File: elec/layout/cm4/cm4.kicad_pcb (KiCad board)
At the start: 2 copper layers, 4 parts, among them CN1 HRSHirose_DF40C_100DS_0_4V51, CN2 HRSHirose_DF40C_100DS_0_4V51, U1 _Texas_Instruments_SN74LVC1G0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

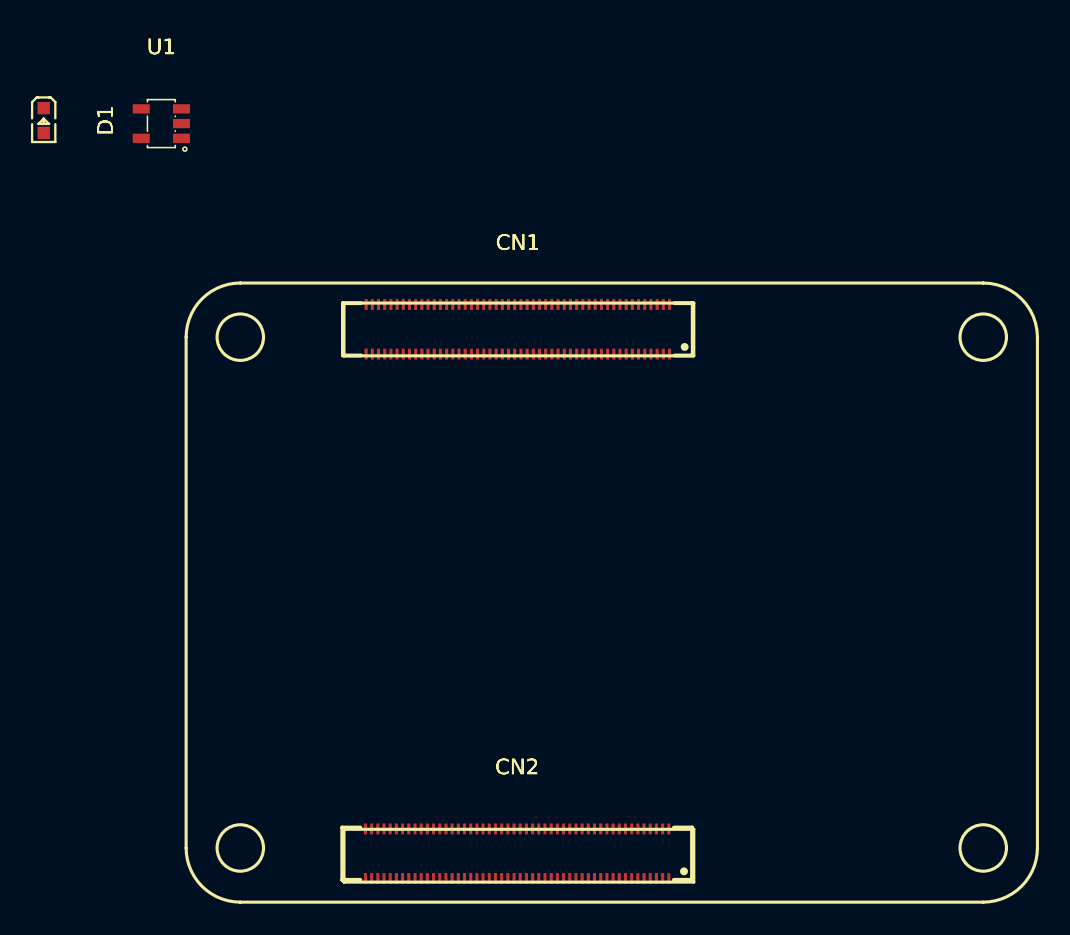
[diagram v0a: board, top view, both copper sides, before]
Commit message: add ethernet connector
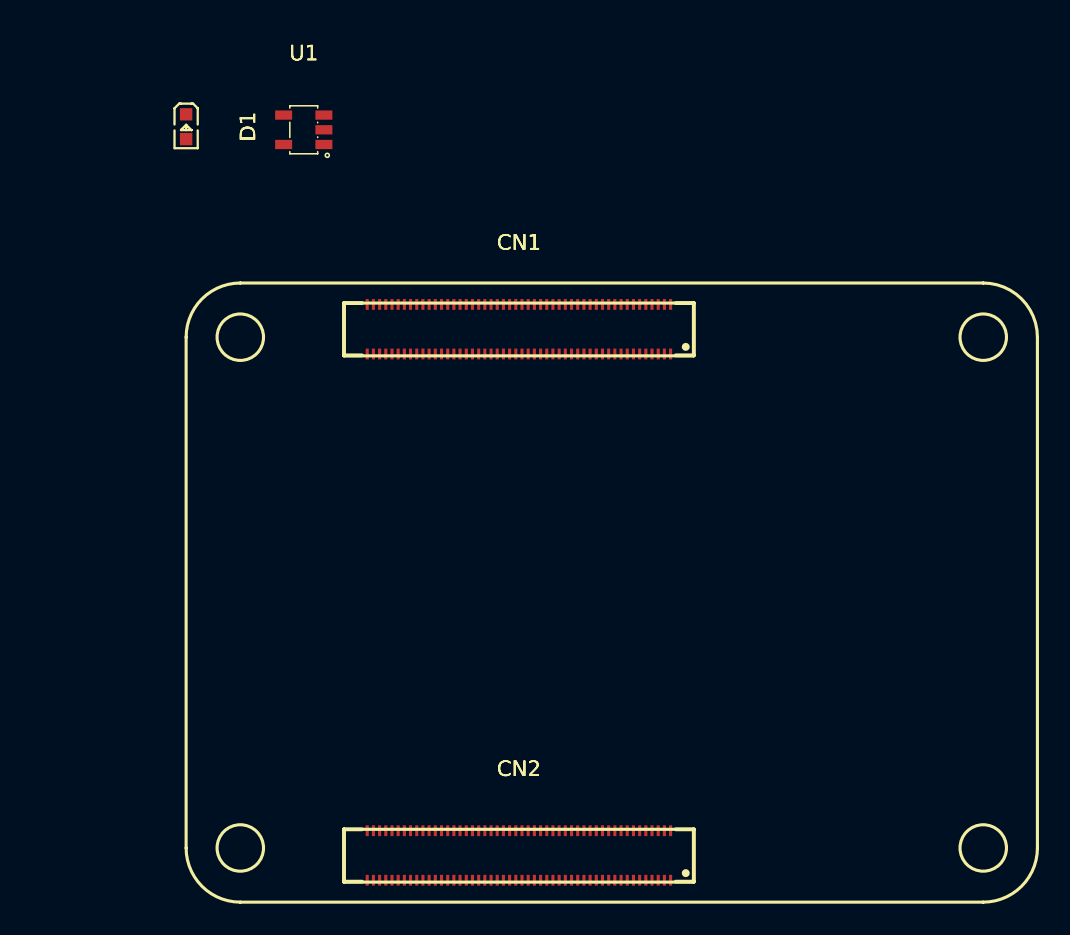
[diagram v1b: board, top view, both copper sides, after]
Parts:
- moved D1 9.21 mm to (128.4, 90.2)
- moved U1 9.21 mm to (136.0, 90.4)
- moved CN2 0.16 mm to (149.9, 137.3)
- moved CN1 0.07 mm to (149.9, 103.3)
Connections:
- net hdi_b-pins[28] renamed HDMI1_D0_P
- net hdi_b-pins[29] renamed HDMI1_D0_N
- net pins[2] renamed ETH_P1_N
- net pins[4] renamed ETH_P0_N
- net signal-11 renamed HDMI1_CEC
- CN1 pad 1: net -> GND
- CN1 pad 10: pins[9] -> pins[19]
- CN1 pad 100: hdi_a-pins[99] -> GND
- CN1 pad 11: pins[10] -> GND
- CN1 pad 12: pins[11] -> signal-2
- CN1 pad 13: net -> I2S_WS
- CN1 pad 14: net -> signal-4
- CN1 pad 15: pins[14] -> signal-3
- CN1 pad 16: hdi_a-pins[15] -> GND
- CN1 pad 17: pins[16] -> signal-1
- CN1 pad 18: hdi_a-pins[17] -> hdi_a-pins[35]
- CN1 pad 19: pins[18] -> pins[37]
- CN1 pad 2: net -> ETH_P1_P
- CN1 pad 20: pins[19] -> pins[39]
- CN1 pad 21: net -> GND
- CN1 pad 22: net -> pins[43]
- CN1 pad 23: net -> pins[45]
- CN1 pad 24: signal-7 -> signal
- CN1 pad 25: signal-4 -> pins[49]
- CN1 pad 26: signal-1 -> GND
- CN1 pad 27: pins[26] -> pins[53]
- CN1 pad 28: pins[27] -> signal-8
- CN1 pad 29: pins[28] -> pins[57]
- CN1 pad 30: pins[29] -> GND
- CN1 pad 31: pins[30] -> pins[61]
- CN1 pad 32: net -> pins[63]
- CN1 pad 33: net -> GND
- CN1 pad 34: signal-5 -> pins[67]
- CN1 pad 35: hdi_a-pins[34] -> pins[69]
- CN1 pad 36: hdi_a-pins[35] -> pins[71]
- CN1 pad 37: pins[36] -> GND
- CN1 pad 38: signal-8 -> pins[75]
- CN1 pad 39: pins[38] -> VCC_3V3
- CN1 pad 4: pins[3] -> GND
- CN1 pad 40: signal-2 -> SCL
- CN1 pad 41: pins[40] -> SDA
- CN1 pad 42: net -> VCC_3V3
- CN1 pad 43: net -> VCC_3V3
- CN1 pad 44: pins[43] -> VCC_1V8
- CN1 pad 45: signal-6 -> VCC_1V8
- CN1 pad 46: pins[45] -> pins[91]
- CN1 pad 47: pins[46] -> hdi_a-pins[93]
- CN1 pad 48: pins[47] -> PWR_LED
- CN1 pad 49: signal-9 -> GND
- CN1 pad 50: pins[49] -> hdi_a-pins[99]
- CN1 pad 51: pins[50] -> hdi_a-pins[98]
- CN1 pad 52: net -> pins[96]
- CN1 pad 53: net -> hdi_a-pins[94]
- CN1 pad 54: signal-10 -> hdi_a-pins[92]
- CN1 pad 55: pins[54] -> pins[90]
- CN1 pad 56: signal-3 -> hdi_a-pins[88]
- CN1 pad 57: hdi_a-pins[56] -> VCC_5V
- CN1 pad 58: signal -> VCC_5V
- CN1 pad 59: net -> VCC_5V
- CN1 pad 6: pins[5] -> ETH_P0_P
- CN1 pad 60: net -> VCC_5V
- CN1 pad 61: pins[60] -> VCC_5V
- CN1 pad 62: pins[61] -> VCC_5V
- CN1 pad 63: hdi_a-pins[62] -> hdi_a-pins[74]
- CN1 pad 64: hdi_a-pins[63] -> pins[72]
- CN1 pad 65: net -> GND
- CN1 pad 66: net -> hdi_a-pins[68]
- CN1 pad 68: pins[67] -> GND
- CN1 pad 69: hdi_a-pins[68] -> hdi_a-pins[62]
- CN1 pad 7: net -> GND
- CN1 pad 70: pins[69] -> pins[60]
- CN1 pad 71: net -> GND
- CN1 pad 72: hdi_a-pins[71] -> hdi_a-pins[56]
- CN1 pad 73: pins[72] -> pins[54]
- CN1 pad 74: net -> GND
- CN1 pad 75: hdi_a-pins[74] -> pins[50]
- CN1 pad 76: pins[75] -> I2S_SCK
- CN1 pad 77: net-1 -> signal-5
- CN1 pad 78: net-2 -> pins[44]-1
- CN1 pad 79: net-1 -> GND
- CN1 pad 8: net -> hdi_a-pins[15]
- CN1 pad 80: pins[79] -> pins[40]
- CN1 pad 81: net-1 -> pins[38]
- CN1 pad 82: pins[81] -> signal-7
- CN1 pad 83: net-1 -> hdi_a-pins[34]
- CN1 pad 84: net-2 -> GND
- CN1 pad 85: net-1 -> pins[30]
- CN1 pad 86: net-2 -> signal-6
- CN1 pad 87: net-1 -> pins[26]
- CN1 pad 88: net-4 -> I2S_SD
- CN1 pad 89: hdi_a-pins[88] -> GND
- CN1 pad 9: pins[8] -> hdi_a-pins[17]
- CN1 pad 90: net-4 -> GND
- CN1 pad 91: pins[90] -> pins[18]
- CN1 pad 92: pins[91] -> ETH_LED_ACTIVITY
- CN1 pad 93: hdi_a-pins[92] -> ETH_LED_LINK
- CN1 pad 94: hdi_a-pins[93] -> GND
- CN1 pad 95: hdi_a-pins[94] -> ETH_P2_P
- CN1 pad 96: net-3 -> ETH_P2_N
- CN1 pad 97: pins[96] -> GND
- CN1 pad 98: net -> ETH_P3_N
- CN1 pad 99: hdi_a-pins[98] -> ETH_P3_P
- CN2 pad 1: pins[0] -> pins[1]
- CN2 pad 10: hdi_b-pins[9] -> GND
- CN2 pad 100: pins[99] -> pins[0]
- CN2 pad 11: hdi_b-pins[10] -> pins[21]
- CN2 pad 12: hdi_b-pins[11] -> pins[23]
- CN2 pad 13: net -> GND
- CN2 pad 14: net -> pins[27]
- CN2 pad 15: hdi_b-pins[14] -> pins[29]
- CN2 pad 16: hdi_b-pins[15] -> GND
- CN2 pad 17: hdi_b-pins[16] -> pins[33]
- CN2 pad 18: hdi_b-pins[17] -> hdi_b-pins[35]
- CN2 pad 19: net -> GND
- CN2 pad 2: pins[1] -> pins[3]
- CN2 pad 20: net -> hdi_b-pins[39]
- CN2 pad 21: pins[20] -> pins[41]
- CN2 pad 22: pins[21] -> GND
- CN2 pad 23: pins[22] -> HDMI1_D2_P
- CN2 pad 24: pins[23] -> HDMI1_D2_N
- CN2 pad 25: net -> hdi_b-pins[49]
- CN2 pad 26: net -> HDMI1_D1_P
- CN2 pad 27: hdi_b-pins[26] -> HDMI1_D1_N
- CN2 pad 28: hdi_b-pins[27] -> GND
- CN2 pad 3: pins[2]-1 -> pins[5]
- CN2 pad 31: net -> GND
- CN2 pad 32: net -> HDMI1_CK_P
- CN2 pad 33: pins[32] -> HDMI1_CK_N
- CN2 pad 34: pins[33] -> GND
- CN2 pad 35: hdi_b-pins[34] -> HDMI0_D2_P
- CN2 pad 36: hdi_b-pins[35] -> HDMI0_D2_N
- CN2 pad 37: net -> GND
- CN2 pad 38: net -> HDMI0_D1_P
- CN2 pad 39: hdi_b-pins[38] -> HDMI0_D1_N
- CN2 pad 4: hdi_b-pins[3] -> GND
- CN2 pad 40: pins[39] -> GND
- CN2 pad 41: hdi_b-pins[40] -> HDMI0_D0_P
- CN2 pad 42: pins[41] -> HDMI0_D0_N
- CN2 pad 43: net -> GND
- CN2 pad 44: net -> HDMI0_CK_P
- CN2 pad 45: pins[44] -> HDMI0_CK_N
- CN2 pad 46: hdi_b-pins[45] -> GND
- CN2 pad 47: pins[46]-1 -> hdi_b-pins[93]
- CN2 pad 48: hdi_b-pins[47] -> pins[95]
- CN2 pad 49: pins[48] -> GND
- CN2 pad 5: pins[4]-1 -> pins[9]
- CN2 pad 50: hdi_b-pins[49] -> pins[99]
- CN2 pad 51: signal-13 -> pins[98]
- CN2 pad 52: pins[51] -> GND
- CN2 pad 53: pins[52] -> hdi_b-pins[94]
- CN2 pad 54: pins[53] -> hdi_b-pins[92]
- CN2 pad 55: net -> GND
- CN2 pad 56: net -> hdi_b-pins[88]
- CN2 pad 57: hdi_b-pins[56] -> pins[86]
- CN2 pad 58: pins[57] -> GND
- CN2 pad 59: pins[58] -> pins[82]
- CN2 pad 6: hdi_b-pins[5] -> pins[11]
- CN2 pad 60: pins[59] -> pins[80]
- CN2 pad 61: net -> GND
- CN2 pad 62: net -> pins[76]
- CN2 pad 63: hdi_b-pins[62] -> hdi_b-pins[74]
- CN2 pad 64: hdi_b-pins[63] -> GND
- CN2 pad 65: pins[64] -> pins[70]
- CN2 pad 66: pins[65] -> hdi_b-pins[68]
- CN2 pad 67: net -> GND
- CN2 pad 68: net -> pins[64]
- CN2 pad 69: hdi_b-pins[68] -> hdi_b-pins[62]
- CN2 pad 7: net -> GND
- CN2 pad 70: signal-17 -> GND
- CN2 pad 71: pins[70] -> pins[58]
- CN2 pad 72: pins[71] -> hdi_b-pins[56]
- CN2 pad 73: net -> GND
- CN2 pad 74: net -> HDMI0_HOTPLUG
- CN2 pad 75: hdi_b-pins[74] -> HDMI0_CEC
- CN2 pad 77: pins[76] -> pins[46]
- CN2 pad 78: signal-15 -> pins[44]
- CN2 pad 79: net -> HDMI1_HOTPLUG
- CN2 pad 8: net -> hdi_b-pins[15]
- CN2 pad 80: net -> hdi_b-pins[40]
- CN2 pad 81: pins[80] -> hdi_b-pins[38]
- CN2 pad 82: signal-12 -> GND
- CN2 pad 83: pins[82] -> hdi_b-pins[34]
- CN2 pad 84: signal-16 -> pins[32]
- CN2 pad 85: net -> GND
- CN2 pad 86: net -> pins[28]
- CN2 pad 87: pins[86] -> hdi_b-pins[26]
- CN2 pad 88: signal-18 -> GND
- CN2 pad 89: hdi_b-pins[88] -> pins[22]
- CN2 pad 9: hdi_b-pins[8] -> hdi_b-pins[17]
- CN2 pad 90: signal-14 -> pins[20]
- CN2 pad 91: net -> GND
- CN2 pad 92: net -> pins[16]
- CN2 pad 93: hdi_b-pins[92] -> pins[14]
- CN2 pad 94: hdi_b-pins[93] -> GND
- CN2 pad 95: hdi_b-pins[94] -> pins[10]
- CN2 pad 96: pins[95] -> pins[8]
- CN2 pad 97: net -> GND
- CN2 pad 98: net -> USB2_D_P
- CN2 pad 99: pins[98] -> USB2_D_N
- D1 pad 1: net-5 -> net
- D1 pad 2: net-2 -> VCC_3V3
- U1 pad 2: net-3 -> PWR_LED
- U1 pad 4: net-5 -> net
- U1 pad 5: net-2 -> VCC_3V3

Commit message: refactor for core updates
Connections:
- net pins[54] renamed signal-11
- CN1 pad 12: signal-2 -> signal-9
- CN1 pad 14: signal-4 -> pins[27]
- CN1 pad 17: signal-1 -> pins[33]
- CN1 pad 24: signal -> pins[47]
- CN1 pad 25: pins[49] -> signal-8
- CN1 pad 27: pins[53] -> signal
- CN1 pad 28: signal-8 -> pins[55]
- CN1 pad 29: pins[57] -> signal-7
- CN1 pad 75: pins[50] -> signal-6
- CN1 pad 77: signal-5 -> signal-10
- CN1 pad 78: pins[44]-1 -> signal-1
- CN1 pad 80: pins[40] -> signal-2
- CN1 pad 81: pins[38] -> signal-4
- CN1 pad 82: signal-7 -> signal-5
- CN1 pad 86: signal-6 -> pins[28]
- CN2 pad 14: pins[27] -> hdi_b-pins[27]
- CN2 pad 17: pins[33] -> hdi_b-pins[33]
- CN2 pad 25: hdi_b-pins[49] -> pins[49]
- CN2 pad 80: hdi_b-pins[40] -> pins[40]
- CN2 pad 81: hdi_b-pins[38] -> pins[38]
- CN2 pad 86: pins[28] -> hdi_b-pins[28]
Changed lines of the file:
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@@
     (net 3 "pins[49]")
     (net 4 "pins[44]")
-    (net 5 "pins[53]")
+    (net 5 "pins[47]")
     (net 6 "hdi_b-pins[62]")
     (net 7 "USB2_D_N")
@@
     (net 19 "ETH_P1_P")
     (net 20 "pins[18]")
-    (net 21 "pins[50]")
-    (net 22 "hdi_b-pins[38]")
+    (net 21 "hdi_b-pins[27]")
+    (net 22 "pins[30]")
     (net 23 "hdi_a-pins[34]")
     (net 24 "pins[67]")
@@
     (net 68 "pins[58]")
     (net 69 "hdi_a-pins[93]")
-    (net 70 "hdi_b-pins[49]")
+    (net 70 "signal-10")
     (net 71 "HDMI1_D2_N")
     (net 72 "HDMI0_D0_P")
@@
     (net 96 "HDMI0_D0_N")
     (net 97 "HDMI1_D0_P")
-    (net 98 "pins[45]")
-    (net 99 "pins[57]")
+    (net 98 "hdi_b-pins[28]")
+    (net 99 "signal-9")
     (net 100 "pins[66]")
     (net 101 "pins[41]")
-    (net 102 "pins[44]-1")
+    (net 102 "signal-11")
     (net 103 "pins[91]")
     (net 104 "hdi_b-pins[88]")
@@
     (net 106 "hdi_b-pins[92]")
     (net 107 "ETH_LED_LINK")
-    (net 108 "pins[30]")
+    (net 108 "pins[45]")
     (net 109 "pins[63]")
     (net 110 "ETH_P1_N")
@@
     (net 112 "signal-5")
     (net 113 "hdi_a-pins[94]")
-    (net 114 "hdi_b-pins[40]")
+    (net 114 "pins[55]")
     (net 115 "signal-3")
     (net 116 "hdi_b-pins[26]")
@@
     (net 130 "hdi_b-pins[15]")
     (net 131 "pins[3]")
-    (net 132 "pins[54]")
+    (net 132 "hdi_b-pins[33]")
     (net 133 "pins[71]")
     (net 134 "pins[21]")
@@
             (layers "F.Cu" "F.Paste" "F.Mask")
             (remove_unused_layers no)
-            (net 28 "pins[27]")
+            (net 21 "hdi_b-pins[27]")
 )
         (pad "15" smd rect
@@
             (layers "F.Cu" "F.Paste" "F.Mask")
             (remove_unused_layers no)
-            (net 105 "pins[33]")
+            (net 132 "hdi_b-pins[33]")
 )
         (pad "18" smd rect
@@
             (layers "F.Cu" "F.Paste" "F.Mask")
             (remove_unused_layers no)
-            (net 70 "hdi_b-pins[49]")
+            (net 3 "pins[49]")
 )
         (pad "26" smd rect
@@
             (layers "F.Cu" "F.Paste" "F.Mask")
             (remove_unused_layers no)
-            (net 114 "hdi_b-pins[40]")
+            (net 89 "pins[40]")
 )
         (pad "81" smd rect
@@
             (layers "F.Cu" "F.Paste" "F.Mask")
             (remove_unused_layers no)
-            (net 22 "hdi_b-pins[38]")
+            (net 141 "pins[38]")
 )
         (pad "82" smd rect
@@
             (layers "F.Cu" "F.Paste" "F.Mask")
             (remove_unused_layers no)
-            (net 139 "pins[28]")
+            (net 98 "hdi_b-pins[28]")
 )
         (pad "87" smd rect
@@
             (layers "F.Cu" "F.Paste" "F.Mask")
             (remove_unused_layers no)
-            (net 26 "signal-2")
+            (net 99 "signal-9")
 )
         (pad "13" smd rect
@@
             (layers "F.Cu" "F.Paste" "F.Mask")
             (remove_unused_layers no)
-            (net 36 "signal-4")
+            (net 28 "pins[27]")
 )
         (pad "15" smd rect
@@
             (layers "F.Cu" "F.Paste" "F.Mask")
             (remove_unused_layers no)
-            (net 10 "signal-1")
+            (net 105 "pins[33]")
 )
         (pad "18" smd rect
@@
             (layers "F.Cu" "F.Paste" "F.Mask")
             (remove_unused_layers no)
-            (net 98 "pins[45]")
+            (net 108 "pins[45]")
 )
         (pad "24" smd rect
@@
             (layers "F.Cu" "F.Paste" "F.Mask")
             (remove_unused_layers no)
-            (net 12 "signal")
+            (net 5 "pins[47]")
 )
         (pad "25" smd rect
@@
             (layers "F.Cu" "F.Paste" "F.Mask")
             (remove_unused_layers no)
-            (net 3 "pins[49]")
+            (net 143 "signal-8")
 )
         (pad "26" smd rect
@@
             (layers "F.Cu" "F.Paste" "F.Mask")
             (remove_unused_layers no)
-            (net 5 "pins[53]")
+            (net 12 "signal")
 )
         (pad "28" smd rect
@@
             (layers "F.Cu" "F.Paste" "F.Mask")
             (remove_unused_layers no)
-            (net 143 "signal-8")
+            (net 114 "pins[55]")
 )
         (pad "29" smd rect
@@
             (layers "F.Cu" "F.Paste" "F.Mask")
             (remove_unused_layers no)
-            (net 99 "pins[57]")
+            (net 61 "signal-7")
 )
         (pad "30" smd rect
@@
             (layers "F.Cu" "F.Paste" "F.Mask")
             (remove_unused_layers no)
-            (net 132 "pins[54]")
+            (net 102 "signal-11")
 )
         (pad "74" smd rect
@@
             (layers "F.Cu" "F.Paste" "F.Mask")
             (remove_unused_layers no)
-            (net 21 "pins[50]")
+            (net 18 "signal-6")
 )
         (pad "76" smd rect
@@
             (layers "F.Cu" "F.Paste" "F.Mask")
             (remove_unused_layers no)
-            (net 112 "signal-5")
+            (net 70 "signal-10")
 )
         (pad "78" smd rect
@@
             (layers "F.Cu" "F.Paste" "F.Mask")
             (remove_unused_layers no)
-            (net 102 "pins[44]-1")
+            (net 10 "signal-1")
 )
         (pad "79" smd rect
@@
             (layers "F.Cu" "F.Paste" "F.Mask")
             (remove_unused_layers no)
-            (net 89 "pins[40]")
+            (net 26 "signal-2")
 )
         (pad "81" smd rect
@@
             (layers "F.Cu" "F.Paste" "F.Mask")
             (remove_unused_layers no)
-            (net 141 "pins[38]")
+            (net 36 "signal-4")
 )
         (pad "82" smd rect
@@
             (layers "F.Cu" "F.Paste" "F.Mask")
             (remove_unused_layers no)
-            (net 61 "signal-7")
+            (net 112 "signal-5")
 )
         (pad "83" smd rect
@@
             (layers "F.Cu" "F.Paste" "F.Mask")
             (remove_unused_layers no)
-            (net 108 "pins[30]")
+            (net 22 "pins[30]")
 )
         (pad "86" smd rect
@@
             (layers "F.Cu" "F.Paste" "F.Mask")
             (remove_unused_layers no)
-            (net 18 "signal-6")
+            (net 139 "pins[28]")
 )
         (pad "87" smd rect
